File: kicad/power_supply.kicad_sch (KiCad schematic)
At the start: 57 parts, among them J10 Phoenix 1987096, J9 USB4105-GF-A, Q1 DMPH6050SK3-13, Q2 BS870, Q3 BS870, U2 FT230XQ, U3 USBLC6-2SC6, U4 LMR51610XDBVR, U6 TXS0102DCUR, U7 AP2127K-ADJTRG1, U8 MCP6001-OT

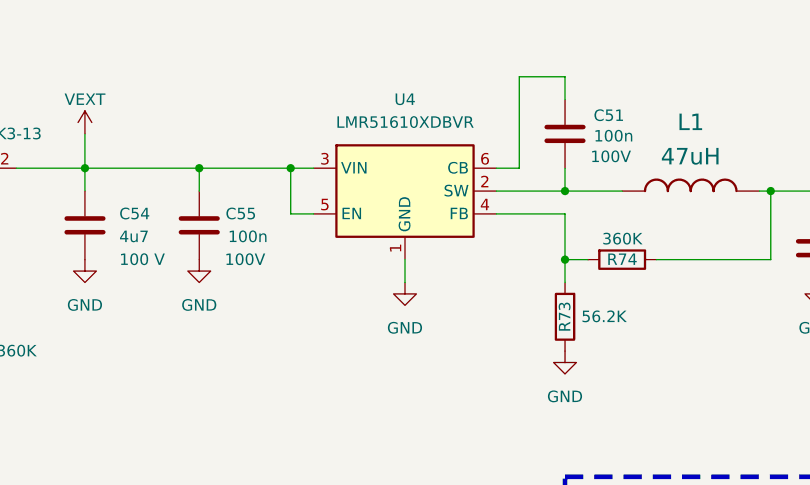
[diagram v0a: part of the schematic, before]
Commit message: fixed layout error on u4
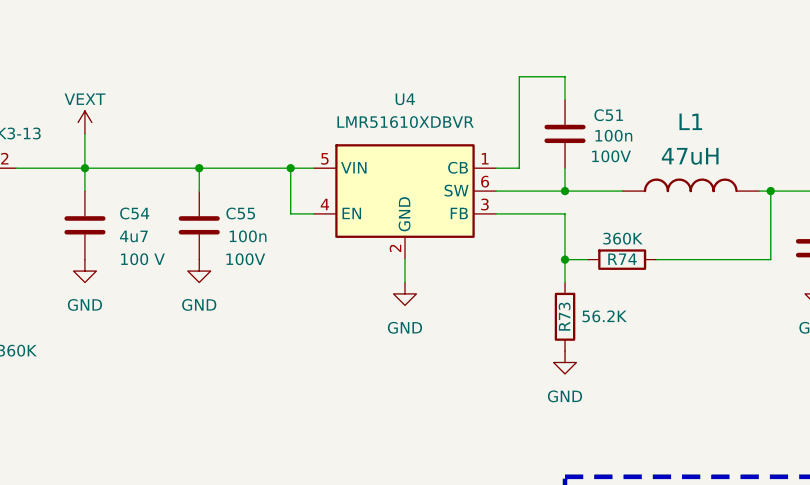
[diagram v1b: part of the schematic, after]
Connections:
- net GND: now also U4.2 (GND); no longer U4.1 (GND)
- net VEXT: now also U4.4 (EN); no longer U4.3 (VIN)
- net at C51.2, L1.1: now also U4.6 (SW); no longer U4.2 (SW)
- net at R73.2, R74.2: now also U4.3 (FB); no longer U4.4 (FB)
- net at C51.1: now also U4.1 (CB); no longer U4.6 (CB)
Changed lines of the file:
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@@
 	(generator_version "8.0")
 	(paper "A4")
+	(title_block
+		(date "2025-01-16")
+		(rev "01")
+	)
 	(junction
 		(at 236.22 114.3)
